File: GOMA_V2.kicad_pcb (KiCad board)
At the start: 2 copper layers, 86.4 x 110.5 mm, 83 parts, among them J10 AudioJack2_SwitchT, J11 AudioJack2_SwitchT, J12 Conn_01x08_Pin, J13 Conn_01x08_Socket, J14 Conn_01x08_Pin, J15 Conn_01x08_Pin, J16 Conn_01x08_Pin, J17 Conn_01x08_Socket, J18 Conn_02x05_Odd_Even, J2 AudioJack2_SwitchT, J3 AudioJack2_SwitchT, J4 AudioJack2_SwitchT, J5 AudioJack2_SwitchT, J6 AudioJack2_SwitchT, J7 Conn_01x08_Socket, J8 AudioJack2_SwitchT, J9 Conn_01x08_Socket, SW1 SW_SPST, SW2 SW_SPST, SW3 SW_SPST, SW4 SW_SPST, U1 LM324, U2 LM78L05_TO92, U3 LM324, U4 LM324, U5 LM324

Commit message: v3 design start
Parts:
- removed J3: AudioJack2_SwitchT, Custom:Thonkiconn mono 3.5mm audio jack PCB spacing
- removed R45: 470, Resistor_THT:R_Axial_DIN0207_L6.3mm_D2.5mm_P10.16mm_Horizontal
- removed U5: LM324, Package_DIP:DIP-14_W7.62mm
- added C10: 100n, Capacitor_THT:C_Disc_D6.0mm_W2.5mm_P5.00mm, F.Cu at (154.9, 134.7)
- added C6: 10n, Capacitor_THT:CP_Radial_D4.0mm_P2.00mm, F.Cu at (285.0, 124.0)
- added C7: 100n, Capacitor_THT:C_Disc_D6.0mm_W2.5mm_P5.00mm, F.Cu at (154.9, 71.1)
- added C8: 100n, Capacitor_THT:C_Disc_D6.0mm_W2.5mm_P5.00mm, F.Cu at (154.9, 94.0)
- added C9: 100n, Capacitor_THT:C_Disc_D6.0mm_W2.5mm_P5.00mm, F.Cu at (154.9, 114.3)
- added J1: ch1 in, Custom:Thonkiconn mono 3.5mm audio jack PCB spacing, F.Cu at (81.3, 165.1)
- added R1: 100k, Resistor_THT:R_Axial_DIN0207_L6.3mm_D2.5mm_P2.54mm_Vertical, F.Cu at (86.4, 76.2)
- added U6: LM78L05_TO92, Package_TO_SOT_THT:TO-92_Inline_Wide, F.Cu at (104.1, 149.9)
- C4: value 10n -> 100n; footprint Capacitor_THT:CP_Radial_D4.0mm_P2.00mm -> Capacitor_THT:C_Disc_D6.0mm_W2.5mm_P5.00mm
- J10: value AudioJack2_SwitchT -> ch3 in
- J11: value AudioJack2_SwitchT -> ch3 out
- J12, J16: moved to F.Cu
- J14: value Conn_01x08_Pin -> ch4 in; footprint Connector_PinHeader_2.54mm:PinHeader_1x08_P2.54mm_Vertical -> Custom:Thonkiconn mono 3.5mm audio jack PCB spacing; moved to F.Cu
- J15: value Conn_01x08_Pin -> ch4 out; footprint Connector_PinHeader_2.54mm:PinHeader_1x08_P2.54mm_Vertical -> Custom:Thonkiconn mono 3.5mm audio jack PCB spacing; moved to F.Cu
- J2: value AudioJack2_SwitchT -> ch1 out
- J4: value AudioJack2_SwitchT -> ch2 in
- J5: value AudioJack2_SwitchT -> ch2 out
- J6, J8: value AudioJack2_SwitchT -> Conn_01x08_Pin; footprint Custom:Thonkiconn mono 3.5mm audio jack PCB spacing -> Connector_PinHeader_2.54mm:PinHeader_1x08_P2.54mm_Vertical
- R10, R32: value 100k -> 1k; footprint Resistor_THT:R_Axial_DIN0207_L6.3mm_D2.5mm_P10.16mm_Horizontal -> Resistor_THT:R_Axial_DIN0207_L6.3mm_D2.5mm_P2.54mm_Vertical
- R11, R17, R20, R42: footprint Resistor_THT:R_Axial_DIN0207_L6.3mm_D2.5mm_P10.16mm_Horizontal -> Resistor_THT:R_Axial_DIN0207_L6.3mm_D2.5mm_P2.54mm_Vertical
- R12, R23, R34: value 22k -> 470; footprint Resistor_THT:R_Axial_DIN0207_L6.3mm_D2.5mm_P2.54mm_Vertical -> Resistor_THT:R_Axial_DIN0207_L6.3mm_D2.5mm_P10.16mm_Horizontal
- R15, R2: value 1k -> 100k; footprint Resistor_THT:R_Axial_DIN0207_L6.3mm_D2.5mm_P10.16mm_Horizontal -> Resistor_THT:R_Axial_DIN0204_L3.6mm_D1.6mm_P2.54mm_Vertical
- R18: footprint Resistor_THT:R_Axial_DIN0207_L6.3mm_D2.5mm_P2.54mm_Vertical -> Resistor_THT:R_Axial_DIN0207_L6.3mm_D2.5mm_P10.16mm_Horizontal
- R21: value 100k -> 1k; footprint Resistor_THT:R_Axial_DIN0204_L3.6mm_D1.6mm_P2.54mm_Vertical -> Resistor_THT:R_Axial_DIN0207_L6.3mm_D2.5mm_P2.54mm_Vertical
- R22, R33, R8: value 470 -> 22k; footprint Resistor_THT:R_Axial_DIN0207_L6.3mm_D2.5mm_P10.16mm_Horizontal -> Resistor_THT:R_Axial_DIN0207_L6.3mm_D2.5mm_P2.54mm_Vertical
- R26, R37: footprint Resistor_THT:R_Axial_DIN0207_L6.3mm_D2.5mm_P10.16mm_Horizontal -> Resistor_THT:R_Axial_DIN0204_L3.6mm_D1.6mm_P2.54mm_Vertical
- R28: value 1k -> 100k; footprint Resistor_THT:R_Axial_DIN0207_L6.3mm_D2.5mm_P10.16mm_Horizontal -> Resistor_THT:R_Axial_DIN0207_L6.3mm_D2.5mm_P2.54mm_Vertical
- R29, R5: footprint Resistor_THT:R_Axial_DIN0204_L3.6mm_D1.6mm_P2.54mm_Vertical -> Resistor_THT:R_Axial_DIN0207_L6.3mm_D2.5mm_P10.16mm_Horizontal
- R31, R39: footprint Resistor_THT:R_Axial_DIN0204_L3.6mm_D1.6mm_P2.54mm_Vertical -> Resistor_THT:R_Axial_DIN0207_L6.3mm_D2.5mm_P2.54mm_Vertical
- R36: footprint Resistor_THT:R_Axial_DIN0207_L6.3mm_D2.5mm_P2.54mm_Vertical -> Resistor_THT:R_Axial_DIN0204_L3.6mm_D1.6mm_P2.54mm_Vertical
- R40: value 1k -> 100k
- R43: value 100k -> 1k
- R7: value 100k -> 470; footprint Resistor_THT:R_Axial_DIN0207_L6.3mm_D2.5mm_P2.54mm_Vertical -> Resistor_THT:R_Axial_DIN0207_L6.3mm_D2.5mm_P10.16mm_Horizontal
- SW1, SW2, SW3, SW4: footprint Custom:SMTS 102 SPDT -> Custom:SMTS 102 SPDT PCB
- U2: value LM78L05_TO92 -> LM324; footprint Package_TO_SOT_THT:TO-92_Inline_Wide -> Package_DIP:DIP-14_W7.62mm
- moved R38 183.6 mm to (284.5, 152.4), turned to 0 degrees
- moved R44 160.1 mm to (276.9, 159.0), turned to 0 degrees
- moved R41 155.3 mm to (276.9, 154.9), turned to 0 degrees
- moved J18 139.9 mm to (304.8, 134.6), turned to 180 degrees
- moved R39 115.6 mm to (276.9, 149.3)
- moved C5 114.9 mm to (285.0, 129.5), turned to 0 degrees
- moved J2 95.5 mm to (81.3, 165.1)
- moved J5 78.7 mm to (91.4, 165.1)
- moved J4 69.0 mm to (91.4, 165.1), turned to 180 degrees
- moved J6 62.6 mm to (73.7, 71.1)
- moved J12 50.8 mm to (78.7, 113.0), turned to 0 degrees
- moved J14 50.2 mm to (111.8, 165.1), turned to 180 degrees
- moved J16 44.1 mm to (114.3, 132.1), turned to 0 degrees
- moved J13 43.6 mm to (139.7, 114.3), turned to 0 degrees
- moved J8 39.2 mm to (119.4, 91.4)
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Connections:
- C1 pad 2: -12V -> GND
- C2 pad 2: -12V -> GND
- C3 pad 2: -12V -> GND
- J10 pad S: GND_FP.4 -> GND_FP
- J10 pad T: Net-(SW4-A) -> Net-(SW3-A)
- J10 pad TN: +5V_FP.4 -> +5V_FP
- J11 pad S: GND_FP.4 -> GND_FP
- J11 pad T: R43_FP -> R32_FP
- J11 pad TN: R39_FP -> R28_FP
- J12 pad 1: R11_FP -> R28_FP
- J12 pad 2: R10_FP -> R32_FP
- J12 pad 3: GND_FP.1 -> GND_FP
- J12 pad 4: U1.5_FP -> U3.5_FP
- J12 pad 5: U1.2_FP -> U3.2_FP
- J12 pad 6: U1.1_FP -> U3.1_FP
- J12 pad 7: U1.6_FP -> U3.6_FP
- J12 pad 8: +5V_FP.1 -> unconnected-(J12-Pin_8-Pad8)
- J13 pad 8: +5V -> unconnected-(J13-Pin_8-Pad8)
- J16 pad 3: GND_FP.4 -> GND_FP
- J16 pad 8: +5V_FP.4 -> +12V_FP
- J17 pad 8: +5V -> +12V
- J2 pad S: GND_FP.1 -> GND_FP
- J2 pad T: Net-(SW1-A) -> R10_FP
- J2 pad TN: +5V_FP.1 -> R11_FP
- J4 pad S: GND_FP.2 -> GND_FP
- J4 pad TN: +5V_FP.2 -> +5V_FP
- J5 pad S: GND_FP.2 -> GND_FP
- J7 pad 8: +5V -> unconnected-(J7-Pin_8-Pad8)
- J9 pad 8: +5V -> unconnected-(J9-Pin_8-Pad8)
- R10 pad 1: Net-(R2-Pad2) -> R10_BP
- R10 pad 2: /Daisy chain in -> Net-(U1A-+)
- R11 pad 1: Net-(R3-Pad2) -> Net-(U2C--)
- R11 pad 2: Net-(U1D--) -> R11_BP
- R12 pad 1: U1.5_FP -> GND_FP
- R12 pad 2: Net-(SW1-A) -> U2.2_FP
- R14 pad 1: Net-(U2D--) -> Net-(U2C--)
- R14 pad 2: Net-(U2A-+) -> Net-(R14-Pad2)
- R15 pad 1: Net-(U2A-+) -> Net-(U2D--)
- R15 pad 2: R21_BP -> Net-(U2A-+)
- R17 pad 1: Net-(R13-Pad2) -> Net-(U3C--)
- R17 pad 2: Net-(U2C--) -> R17_BP
- R18 pad 1: Net-(U3C--) -> Net-(R13-Pad2)
- R18 pad 2: R17_BP -> Net-(U2C--)
- R19 pad 1: GND_FP.2 -> U2.5_FP
- R19 pad 2: U2.5_FP -> Net-(SW2-A)
- R2 pad 1: Net-(U1A-+) -> U1.6_BP
- R2 pad 2: R10_BP -> Net-(R2-Pad2)
- R21 pad 1: Net-(U2C--) -> R21_BP
- R21 pad 2: Net-(R14-Pad2) -> Net-(U2A-+)
- R22 pad 1: GND_FP.2 -> GND_FP
- R22 pad 2: U2.2_FP -> U2.5_FP
- R23 pad 1: U2.5_FP -> GND_FP
- R23 pad 2: Net-(SW2-A) -> U3.2_FP
- R24 pad 1: Net-(U3D--) -> U3.6_BP
- R24 pad 2: Net-(U3A-+) -> Net-(R24-Pad2)
- R26 pad 1: Net-(R25-Pad2) -> Net-(U3D--)
- R26 pad 2: Net-(U3D--) -> Net-(U3A-+)
- R28 pad 1: Net-(U3A-+) -> Net-(U4C--)
- R28 pad 2: R32_BP -> R28_BP
- R29 pad 1: Net-(U4D--) -> Net-(R24-Pad2)
- R29 pad 2: Net-(U4A-+) -> Net-(U3C--)
- R3 pad 1: Net-(U1D--) -> /Daisy chain in
- R3 pad 2: Net-(U1A-+) -> Net-(R3-Pad2)
- R30 pad 1: GND_FP.3 -> U3.5_FP
- R30 pad 2: U3.5_FP -> Net-(SW3-A)
- R31 pad 1: U3.6_BP -> Net-(R25-Pad2)
- R31 pad 2: Net-(R24-Pad2) -> Net-(U3D--)
- R32 pad 1: Net-(R24-Pad2) -> R32_BP
- R32 pad 2: Net-(U3C--) -> Net-(U3A-+)
- R33 pad 1: GND_FP.3 -> GND_FP
- R33 pad 2: U3.2_FP -> U3.5_FP
- R34 pad 1: U3.5_FP -> GND_FP
- R34 pad 2: Net-(SW3-A) -> U4.2_FP
- R35 pad 1: Net-(U4C--) -> U4.6_BP
- R35 pad 2: Net-(R36-Pad2) -> Net-(R35-Pad2)
- R36 pad 2: R28_BP -> Net-(R36-Pad2)
- R37 pad 1: Net-(R36-Pad2) -> Net-(U4D--)
- R37 pad 2: Net-(U4D--) -> Net-(U4A-+)
- R39 pad 1: U4.6_BP -> /Daisy chain out
- R39 pad 2: Net-(R35-Pad2) -> R39_BP
- R4 pad 1: U1.6_BP -> Net-(U1D--)
- R4 pad 2: Net-(R2-Pad2) -> Net-(U1A-+)
- R40 pad 1: Net-(U4A-+) -> Net-(R35-Pad2)
- R40 pad 2: R43_BP -> Net-(U4C--)
- R41 pad 1: GND_FP.4 -> U4.5_FP
- R41 pad 2: U4.5_FP -> Net-(SW4-A)
- R42 pad 1: Net-(R35-Pad2) -> Net-(R36-Pad2)
- R42 pad 2: Net-(U4C--) -> Net-(U4D--)
- R43 pad 1: /Daisy chain out -> R43_BP
- R43 pad 2: R39_BP -> Net-(U4A-+)
- R44 pad 1: U4.5_FP -> GND_FP
- R44 pad 2: Net-(SW4-A) -> U4.5_FP
- R5 pad 1: /Daisy chain in -> Net-(R2-Pad2)
- R5 pad 2: Net-(R3-Pad2) -> /Daisy chain in
- R6 pad 1: Net-(U2C--) -> Net-(R3-Pad2)
- R6 pad 2: R11_BP -> Net-(U1D--)
- R7 pad 1: Net-(SW1-B) -> GND_FP
- R7 pad 2: U1.6_FP -> U1.2_FP
- R8 pad 1: GND_FP.1 -> U1.5_FP
- R8 pad 2: U1.2_FP -> Net-(SW1-A)
- R9 pad 1: GND_FP.1 -> GND_FP
- RV1 pad 1: GND_FP.1 -> GND_FP
- RV2 pad 1: GND_FP.2 -> GND_FP
- RV3 pad 1: GND_FP.3 -> GND_FP
- RV4 pad 1: GND_FP.4 -> GND_FP
- U2 pad 1: +5V -> U2.1_BP
- U2 pad 2: GND -> U2.2_BP
- U2 pad 3: +12V -> Net-(U2A-+)
- U3 pad 1: U2.1_BP -> U3.1_BP
- U3 pad 13: Net-(U2D--) -> Net-(U3D--)
- U3 pad 14: Net-(U2A-+) -> Net-(U3A-+)
- U3 pad 2: U2.2_BP -> U3.2_BP
- U3 pad 3: Net-(U2A-+) -> Net-(U3A-+)
- U3 pad 5: U2.5_BP -> U3.5_BP
- U3 pad 6: U2.6_BP -> U3.6_BP
- U3 pad 7: Net-(R13-Pad2) -> Net-(R24-Pad2)
- U3 pad 8: Net-(R14-Pad2) -> Net-(R25-Pad2)
- U3 pad 9: Net-(U2C--) -> Net-(U3C--)
- U4 pad 1: U3.1_BP -> U4.1_BP
- U4 pad 13: Net-(U3D--) -> Net-(U4D--)
- U4 pad 14: Net-(U3A-+) -> Net-(U4A-+)
- U4 pad 2: U3.2_BP -> U4.2_BP
- U4 pad 3: Net-(U3A-+) -> Net-(U4A-+)
- U4 pad 5: U3.5_BP -> U4.5_BP
- U4 pad 6: U3.6_BP -> U4.6_BP
- U4 pad 7: Net-(R24-Pad2) -> Net-(R35-Pad2)
- U4 pad 8: Net-(R25-Pad2) -> Net-(R36-Pad2)
- U4 pad 9: Net-(U3C--) -> Net-(U4C--)
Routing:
- net GND: track 195.0 -> 0.00 mm, vias 2 -> 0
- net -12V: track 195.6 -> 10.3 mm, vias 7 -> 0
- net +12V: track 168.2 -> 10.2 mm, vias 9 -> 0
- net +5V: track 88.9 -> 0.00 mm
- net GND_FP.4: track 67.2 -> 0.00 mm, vias 2 -> 0
- net Net-(SW4-A): track 47.7 -> 0.00 mm
- net +5V_FP: track 0.00 -> 46.3 mm
- net GND_FP.2: track 43.2 -> 0.00 mm, vias 1 -> 0
- net GND_FP.1: track 43.2 -> 0.00 mm, vias 1 -> 0
- net GND_FP.3: track 43.2 -> 0.00 mm, vias 1 -> 0
- net +5V_FP.4: track 33.0 -> 0.00 mm, vias 1 -> 0
- net +5V_FP.3: track 33.0 -> 0.00 mm, vias 1 -> 0
- net +5V_FP.2: track 33.0 -> 0.00 mm, vias 1 -> 0
- net +5V_FP.1: track 33.0 -> 0.00 mm, vias 1 -> 0
- net GND_FP: track 0.00 -> 30.5 mm
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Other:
- board outline removed
- board text removed: "+"
- board text removed: "Daisy chain in"
- board text removed: "Daisy chain out"
- board text removed: "±"

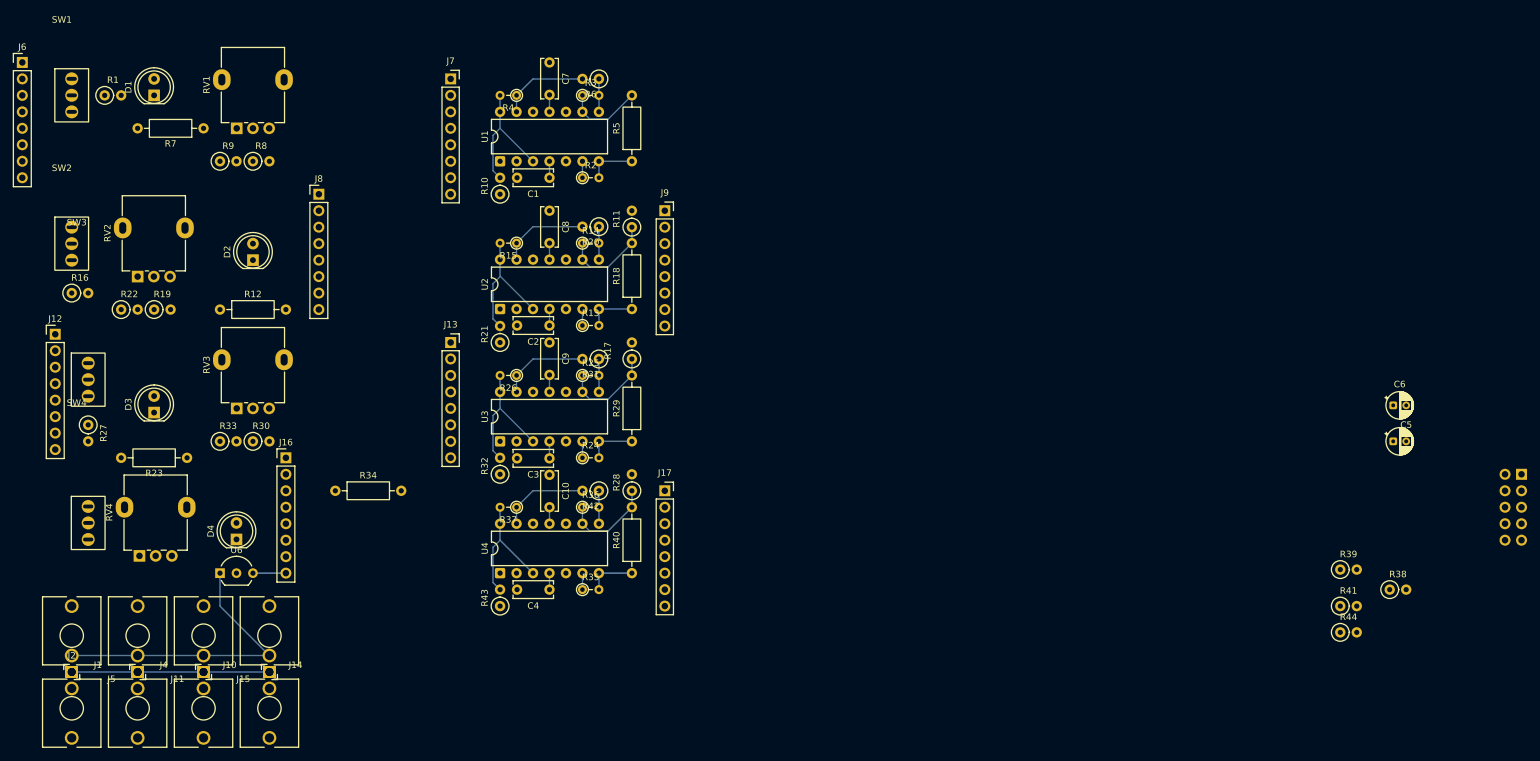
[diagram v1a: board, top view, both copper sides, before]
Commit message: bottom PCB routing
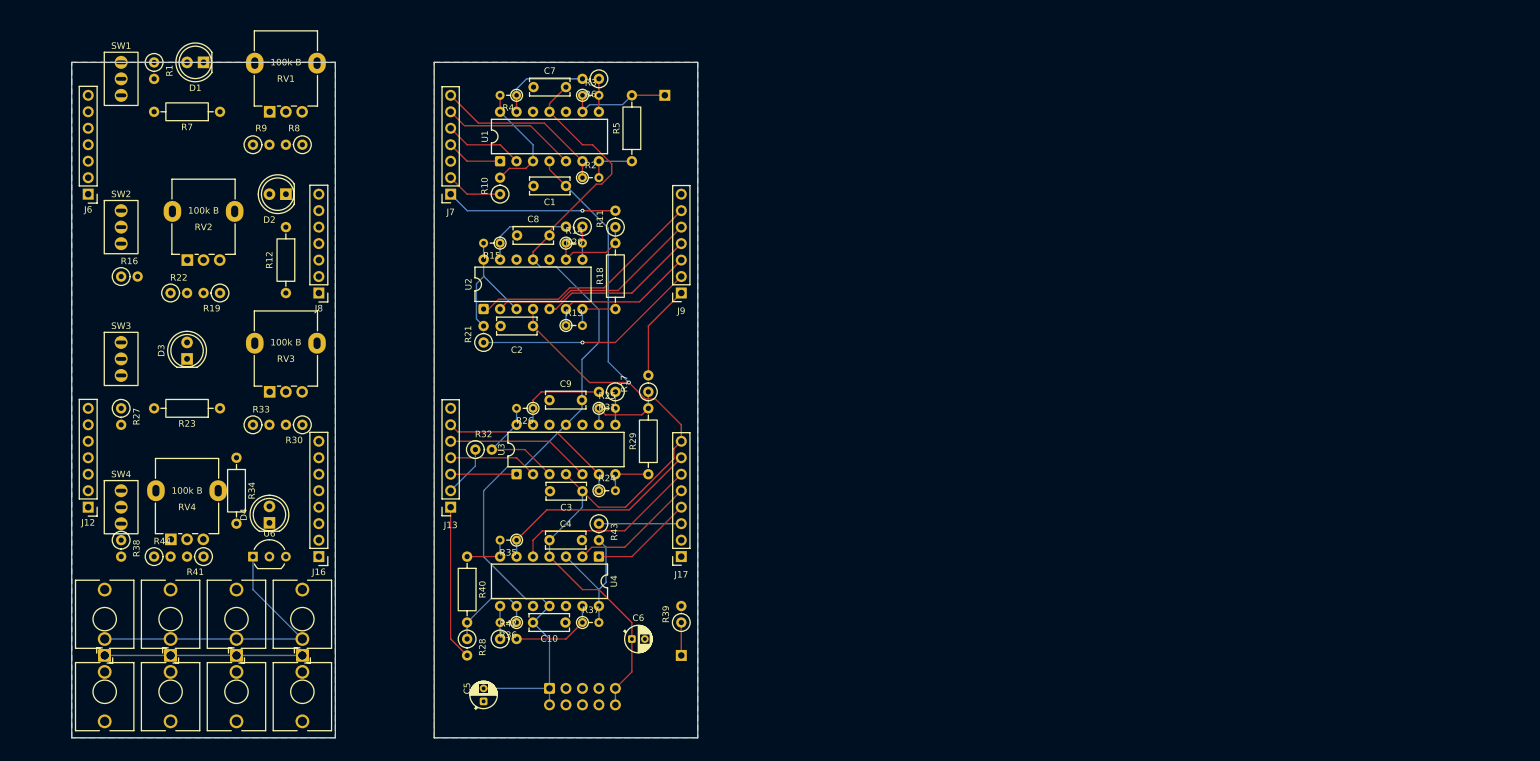
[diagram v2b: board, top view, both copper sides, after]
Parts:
- added J19: Daisy out, Connector_PinHeader_2.54mm:PinHeader_1x01_P2.54mm_Vertical, B.Cu at (175.3, 162.6)
- added J3: Daisy in, Connector_PinHeader_2.54mm:PinHeader_1x01_P2.54mm_Vertical, B.Cu at (172.7, 76.2)
- J12, J6, J8: value Conn_01x08_Pin -> Conn_01x07_Pin; footprint Connector_PinHeader_2.54mm:PinHeader_1x08_P2.54mm_Vertical -> Connector_PinHeader_2.54mm:PinHeader_1x07_P2.54mm_Vertical
- J13, J7, J9: value Conn_01x08_Socket -> Conn_01x07_Socket; footprint Connector_PinSocket_2.54mm:PinSocket_1x08_P2.54mm_Vertical -> Connector_PinSocket_2.54mm:PinSocket_1x07_P2.54mm_Vertical
- J18: footprint Connector_PinHeader_2.54mm:PinHeader_2x05_P2.54mm_Vertical -> Connector_IDC:IDC-Header_2x05_P2.54mm_Vertical
- moved R38 195.7 mm to (88.9, 144.8), turned to -90 degrees
- moved R44 183.3 mm to (94.0, 147.3)
- moved R41 175.4 mm to (101.6, 147.3), turned to 180 degrees
- moved J18 153.5 mm to (154.9, 167.6), turned to -90 degrees
- moved C5 145.9 mm to (144.8, 169.6), turned to 90 degrees
- moved C6 122.8 mm to (167.6, 160.0)
- moved R39 101.9 mm to (175.3, 157.5), turned to 90 degrees
- moved R28 34.2 mm to (142.2, 160.0), turned to -90 degrees
- moved R42 27.5 mm to (147.3, 160.0), turned to 0 degrees
- moved J12 27.1 mm to (83.8, 139.7), turned to 180 degrees
- moved R40 25.5 mm to (142.2, 147.3), turned to -90 degrees
- moved J13 25.4 mm to (139.7, 139.7), turned to 180 degrees
- moved C10 22.9 mm to (157.4, 157.5), turned to 180 degrees
- moved J6 22.7 mm to (83.8, 91.4), turned to 180 degrees
- moved R36 20.5 mm to (149.9, 157.5), turned to 180 degrees
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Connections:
- net /Daisy chain in renamed Net-(J3-Pin_1)
- J12 pad 3: GND_FP -> U3.1_FP
- J12 pad 4: U3.5_FP -> U3.2_FP
- J12 pad 5: U3.2_FP -> U3.5_FP
- J12 pad 6: U3.1_FP -> U3.6_FP
- J12 pad 7: U3.6_FP -> GND_FP
- J13 pad 3: GND -> U3.1_BP
- J13 pad 4: U3.5_BP -> U3.2_BP
- J13 pad 5: U3.2_BP -> U3.5_BP
- J13 pad 6: U3.1_BP -> U3.6_BP
- J13 pad 7: U3.6_BP -> GND
- J16 pad 2: R43_FP -> GND_FP
- J16 pad 3: GND_FP -> R43_FP
- J16 pad 4: U4.5_FP -> U4.1_FP
- J16 pad 6: U4.1_FP -> U4.5_FP
- J17 pad 2: R43_BP -> GND
- J17 pad 3: GND -> R43_BP
- J17 pad 4: U4.5_BP -> U4.1_BP
- J17 pad 6: U4.1_BP -> U4.5_BP
- J6 pad 4: U1.5_FP -> U1.1_FP
- J6 pad 6: U1.1_FP -> U1.5_FP
- J7 pad 4: U1.5_BP -> U1.1_BP
- J7 pad 6: U1.1_BP -> U1.5_BP
- J8 pad 3: GND_FP -> U2.6_FP
- J8 pad 7: U2.6_FP -> GND_FP
- J9 pad 3: GND -> U2.6_BP
- J9 pad 7: U2.6_BP -> GND
- R19 pad 1: U2.5_FP -> Net-(SW2-A)
- R19 pad 2: Net-(SW2-A) -> U2.5_FP
- R30 pad 1: U3.5_FP -> Net-(SW3-A)
- R30 pad 2: Net-(SW3-A) -> U3.5_FP
- R39 pad 1: /Daisy chain out -> Net-(J19-Pin_1)
- R41 pad 1: U4.5_FP -> Net-(SW4-A)
- R41 pad 2: Net-(SW4-A) -> U4.5_FP
- R8 pad 1: U1.5_FP -> Net-(SW1-A)
- R8 pad 2: Net-(SW1-A) -> U1.5_FP
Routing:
- net +12V: track 10.2 -> 141.3 mm, vias 0 -> 1
- net -12V: track 10.3 -> 138.5 mm
- net U2.1_BP: track 0.00 -> 36.8 mm
- net R21_BP: track 0.00 -> 34.7 mm, vias 0 -> 1
- net U2.2_BP: track 0.00 -> 33.2 mm
- net U4.6_BP: track 2.54 -> 33.2 mm
- net U4.5_BP: track 0.00 -> 29.6 mm
- net R11_BP: track 0.00 -> 26.5 mm, vias 0 -> 1
- net U3.6_BP: track 2.54 -> 28.6 mm
- net U1.6_BP: track 2.54 -> 27.1 mm
- net U2.5_BP: track 0.00 -> 24.5 mm
- net R28_BP: track 0.00 -> 23.9 mm
- net U3.5_BP: track 0.00 -> 22.4 mm
- net U1.5_BP: track 0.00 -> 20.9 mm
- net U2.6_BP: track 2.54 -> 23.4 mm
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- added copper zone on B.Cu, net GND
- added copper zone on B.Cu, net GND_FP
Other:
- board outline added: 96.5 x 104.1 mm

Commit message: bottom PCB routing
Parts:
- moved C10 5.00 mm to (152.4, 157.5), turned to 0 degrees
- turned C4 to 90 degrees
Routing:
- net R39_BP: track 0.00 -> 7.62 mm
- net Net-(U2D--): track 14.3 -> 15.8 mm, vias 0 -> 1
- net -12V: track 138.5 -> 139.9 mm

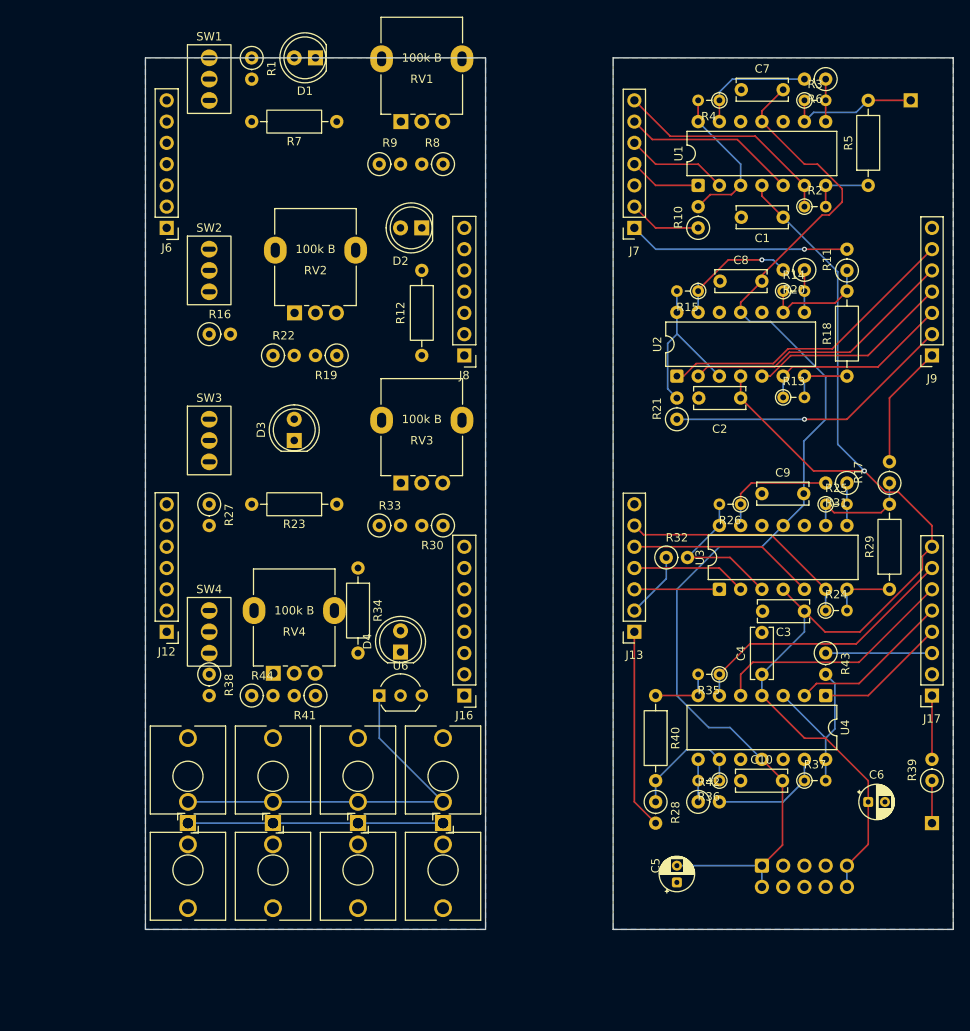
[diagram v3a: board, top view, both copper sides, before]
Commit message: routing complete, DRC passes
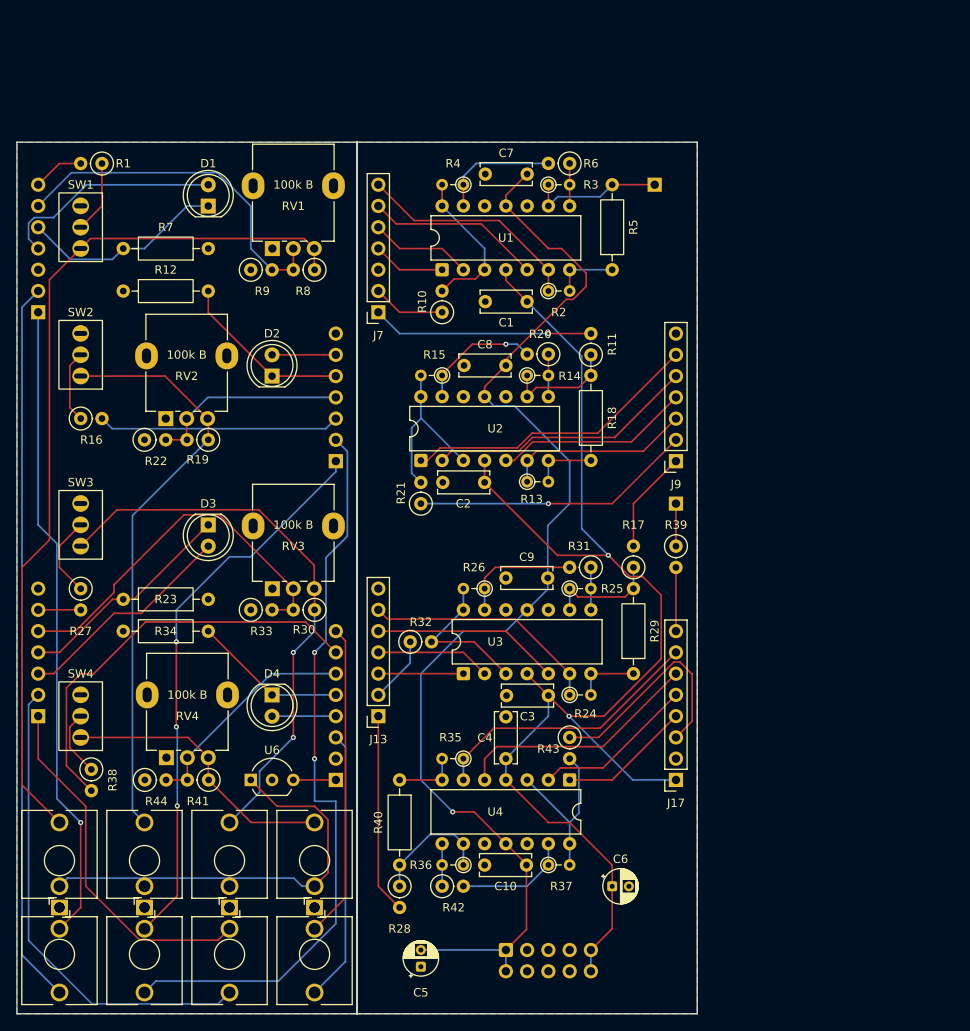
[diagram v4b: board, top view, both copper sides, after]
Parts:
- J12, J16, J6, J8: moved to B.Cu
- moved J19 48.9 mm to (144.7, 124.4), turned to 180 degrees
- moved R39 41.5 mm to (144.7, 129.5), turned to -90 degrees
- moved R12 35.8 mm to (78.6, 99.0), turned to 0 degrees
- moved J9 33.1 mm to (144.7, 119.3)
- moved C10 32.2 mm to (121.8, 167.6)
- moved C2 32.2 mm to (121.8, 121.8)
- moved C3 32.2 mm to (129.4, 147.3)
- moved C5 32.2 mm to (114.2, 179.7)
- moved J3 32.2 mm to (142.1, 86.3)
- moved R11 32.2 mm to (134.5, 106.6)
- moved R17 32.2 mm to (139.6, 132.0)
- moved R18 32.2 mm to (134.5, 119.2)
- moved R2 32.2 mm to (129.4, 99.0)
- moved R20 32.2 mm to (129.4, 106.5)
- moved R21 32.2 mm to (114.2, 124.4)
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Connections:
- J16 pad 1: R39_FP -> +12V_FP
- J16 pad 8: +12V_FP -> R39_FP
- J17 pad 1: R39_BP -> +12V
- J17 pad 8: +12V -> R39_BP
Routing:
- net Net-(SW1-A): track 0.00 -> 104.7 mm
- net R21_FP: track 0.00 -> 88.8 mm, vias 0 -> 2
- net R10_FP: track 0.00 -> 86.5 mm
- net R11_FP: track 0.00 -> 76.8 mm, vias 0 -> 1
- net Net-(SW2-A): track 0.00 -> 69.8 mm
- net Net-(SW3-A): track 0.00 -> 67.3 mm, vias 0 -> 2
- net R17_FP: track 0.00 -> 66.9 mm, vias 0 -> 3
- net R32_FP: track 0.00 -> 57.5 mm
- net U4.6_FP: track 0.00 -> 50.5 mm
- net U3.5_FP: track 0.00 -> 45.5 mm
- net R28_FP: track 0.00 -> 43.1 mm
- net U1.5_FP: track 0.00 -> 42.4 mm
- net R39_FP: track 0.00 -> 37.6 mm
- net Net-(SW4-A): track 0.00 -> 33.6 mm
- net R43_FP: track 0.00 -> 32.5 mm
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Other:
- board size 96.5 x 104.1 mm -> 81.3 x 104.1 mm
- board text removed: "128.5mm"
- board text removed: "45.7mm"
